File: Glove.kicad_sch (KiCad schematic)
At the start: 39 parts

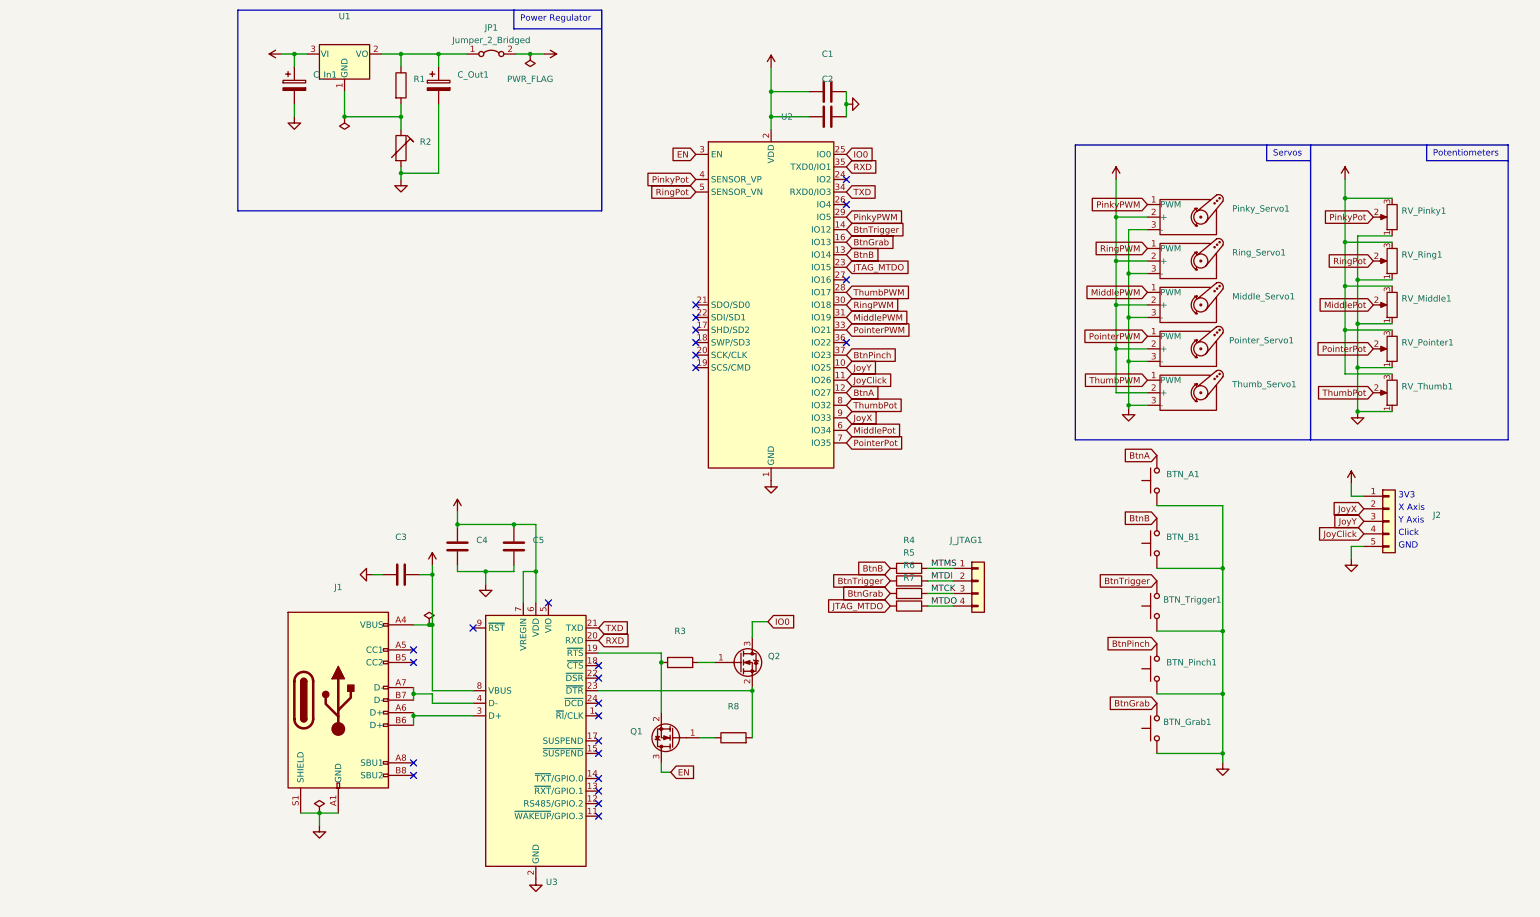
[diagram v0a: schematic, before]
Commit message: Remove Voltage Divider from Power Supply
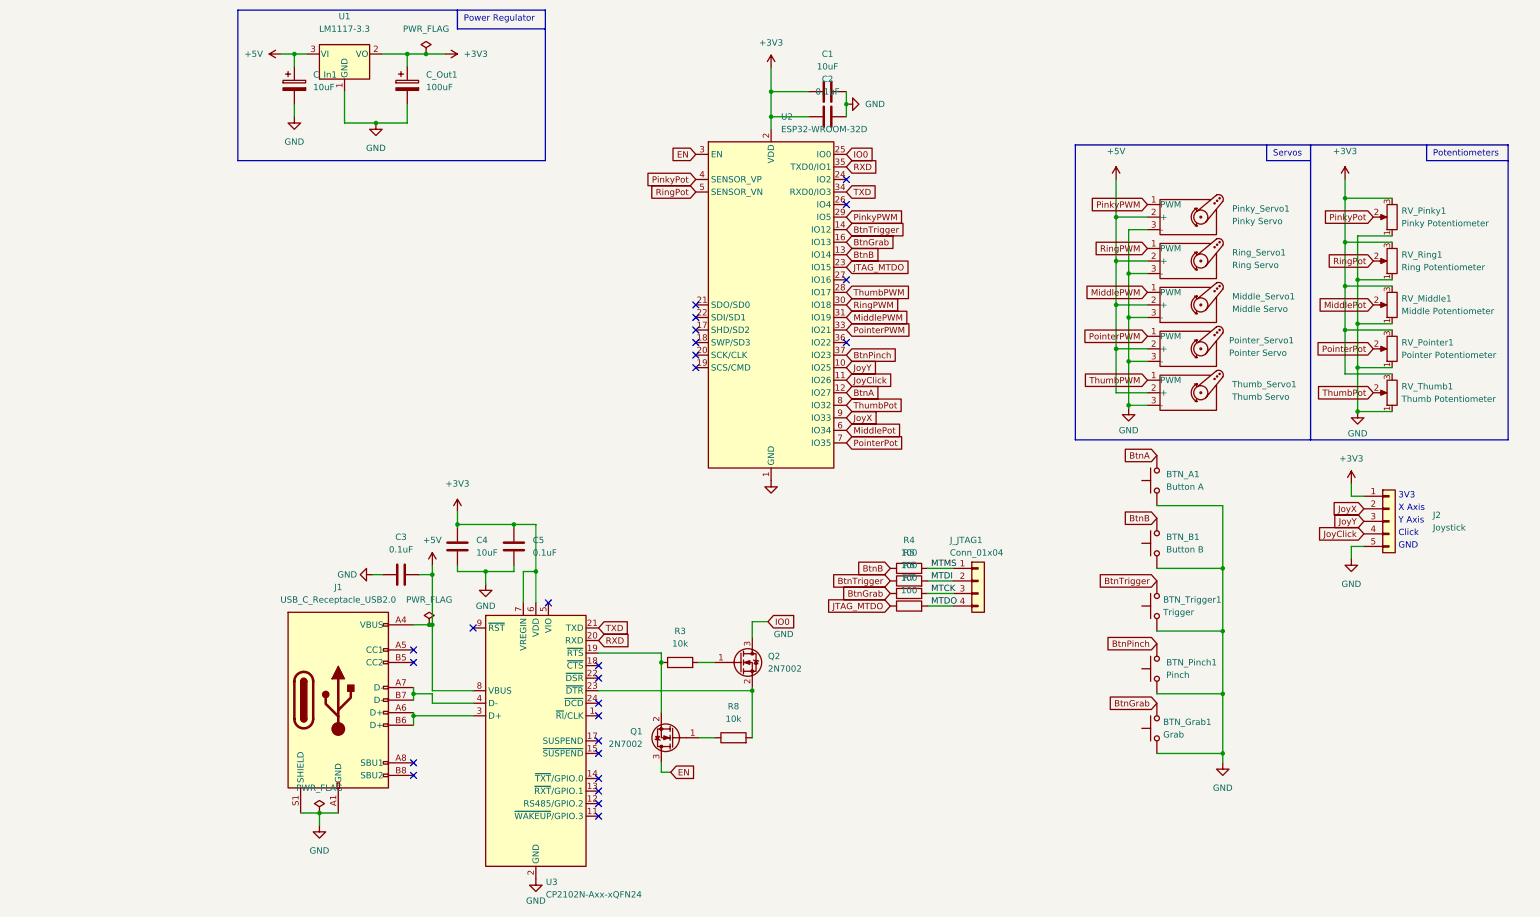
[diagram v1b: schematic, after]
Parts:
- removed JP1: Jumper_2_Bridged, Connector_PinHeader_2.54mm:PinHeader_1x02_P2.54mm_Vertical, symbol Jumper:Jumper_2_Bridged
- removed R1: (no value), symbol Device:R
- removed R2: (no value), symbol Device:R_Trim
- BTN_A1: value (none) -> Button A; footprint (none) -> Connector_JST:JST_XH_B2B-XH-A_1x02_P2.50mm_Vertical
- BTN_B1: value (none) -> Button B; footprint (none) -> Connector_JST:JST_XH_B2B-XH-A_1x02_P2.50mm_Vertical
- BTN_Grab1: value (none) -> Grab; footprint (none) -> Connector_JST:JST_XH_B2B-XH-A_1x02_P2.50mm_Vertical
- BTN_Pinch1: value (none) -> Pinch; footprint (none) -> Connector_JST:JST_XH_B2B-XH-A_1x02_P2.50mm_Vertical
- BTN_Trigger1: value (none) -> Trigger; footprint (none) -> Connector_JST:JST_XH_B2B-XH-A_1x02_P2.50mm_Vertical
- C1, C4, C_In1: value (none) -> 10uF; footprint (none) -> Capacitor_SMD:C_0805_2012Metric_Pad1.18x1.45mm_HandSolder
- C2, C3, C5: value (none) -> 0.1uF; footprint (none) -> Capacitor_SMD:C_0805_2012Metric_Pad1.18x1.45mm_HandSolder
- C_Out1: value (none) -> 100uF; footprint (none) -> Capacitor_SMD:C_0805_2012Metric_Pad1.18x1.45mm_HandSolder
- J1: value (none) -> USB_C_Receptacle_USB2.0; footprint (none) -> Connector_USB:USB_C_Receptacle_XKB_U262-16XN-4BVC11
- J2: value (none) -> Joystick; footprint (none) -> Connector_JST:JST_XH_B5B-XH-A_1x05_P2.50mm_Vertical
- J_JTAG1: value (none) -> Conn_01x04; footprint (none) -> Connector_PinHeader_2.54mm:PinHeader_1x04_P2.54mm_Vertical
- Middle_Servo1: value (none) -> Middle Servo; footprint (none) -> Connector_JST:JST_XH_B3B-XH-A_1x03_P2.50mm_Vertical
- Pinky_Servo1: value (none) -> Pinky Servo; footprint (none) -> Connector_JST:JST_XH_B3B-XH-A_1x03_P2.50mm_Vertical
- Pointer_Servo1: value (none) -> Pointer Servo; footprint (none) -> Connector_JST:JST_XH_B3B-XH-A_1x03_P2.50mm_Vertical
- Q1, Q2: value (none) -> 2N7002; footprint (none) -> Package_TO_SOT_SMD:SOT-23
- R3, R8: value (none) -> 10k; footprint (none) -> Resistor_SMD:R_0805_2012Metric_Pad1.20x1.40mm_HandSolder
- R4, R5, R6, R7: value (none) -> 100; footprint (none) -> Resistor_SMD:R_0805_2012Metric_Pad1.20x1.40mm_HandSolder
- RV_Middle1: value (none) -> Middle Potentiometer; footprint (none) -> Connector_JST:JST_XH_B3B-XH-A_1x03_P2.50mm_Vertical
- RV_Pinky1: value (none) -> Pinky Potentiometer; footprint (none) -> Connector_JST:JST_XH_B3B-XH-A_1x03_P2.50mm_Vertical
- RV_Pointer1: value (none) -> Pointer Potentiometer; footprint (none) -> Connector_JST:JST_XH_B3B-XH-A_1x03_P2.50mm_Vertical
- RV_Ring1: value (none) -> Ring Potentiometer; footprint (none) -> Connector_JST:JST_XH_B3B-XH-A_1x03_P2.50mm_Vertical
- RV_Thumb1: value (none) -> Thumb Potentiometer; footprint (none) -> Connector_JST:JST_XH_B3B-XH-A_1x03_P2.50mm_Vertical
- Ring_Servo1: value (none) -> Ring Servo; footprint (none) -> Connector_JST:JST_XH_B3B-XH-A_1x03_P2.50mm_Vertical
- Thumb_Servo1: value (none) -> Thumb Servo; footprint (none) -> Connector_JST:JST_XH_B3B-XH-A_1x03_P2.50mm_Vertical
- U1: value (none) -> LM1117-3.3; footprint (none) -> Package_TO_SOT_SMD:SOT-223
- U2: value (none) -> ESP32-WROOM-32D; footprint (none) -> RF_Module:ESP32-WROOM-32
- U3: value (none) -> CP2102N-Axx-xQFN24; footprint (none) -> Package_DFN_QFN:QFN-24-1EP_4x4mm_P0.5mm_EP2.6x2.6mm
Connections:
- net +3V3: now also C_Out1.1, U1.2 (VO)
- net GND: now also U1.1 (GND)
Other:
- moved on the sheet: C_Out1

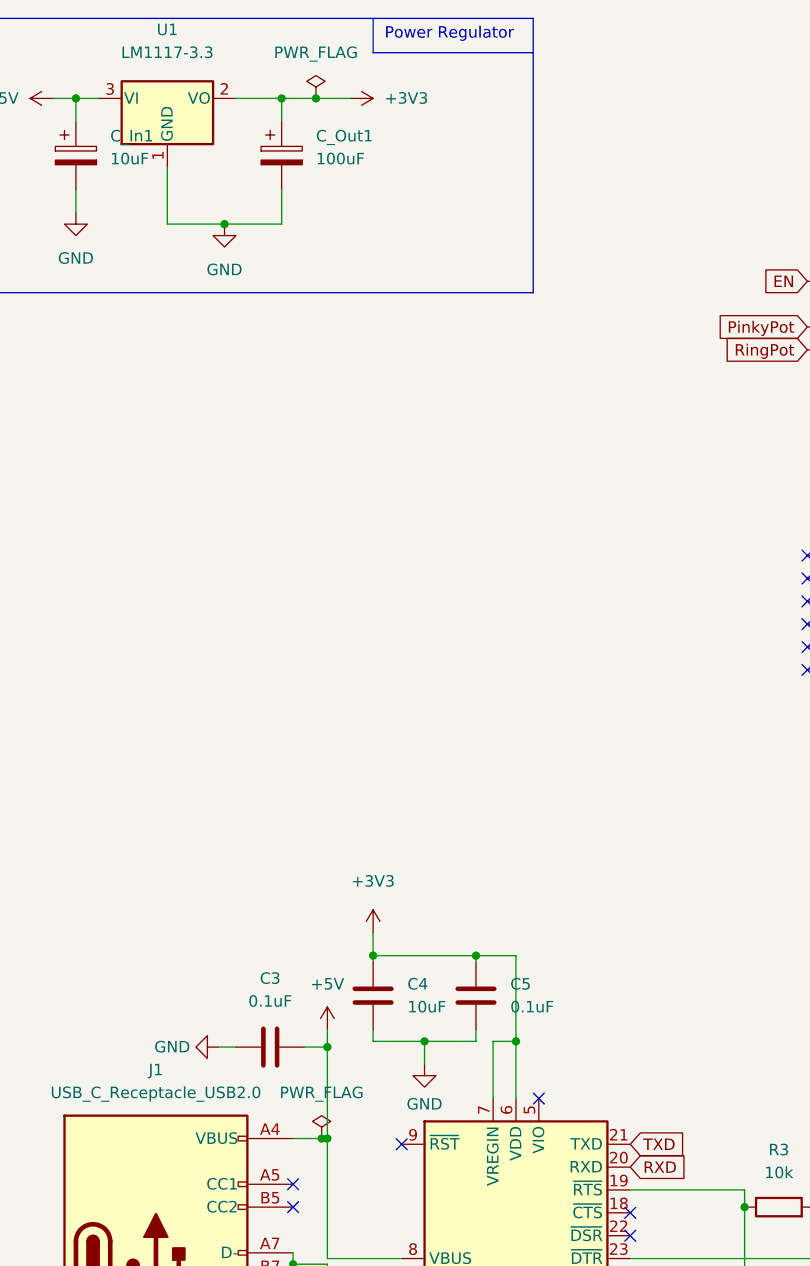
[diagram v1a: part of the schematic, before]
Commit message: Connect VIO to 3.3v for CP2102 chip
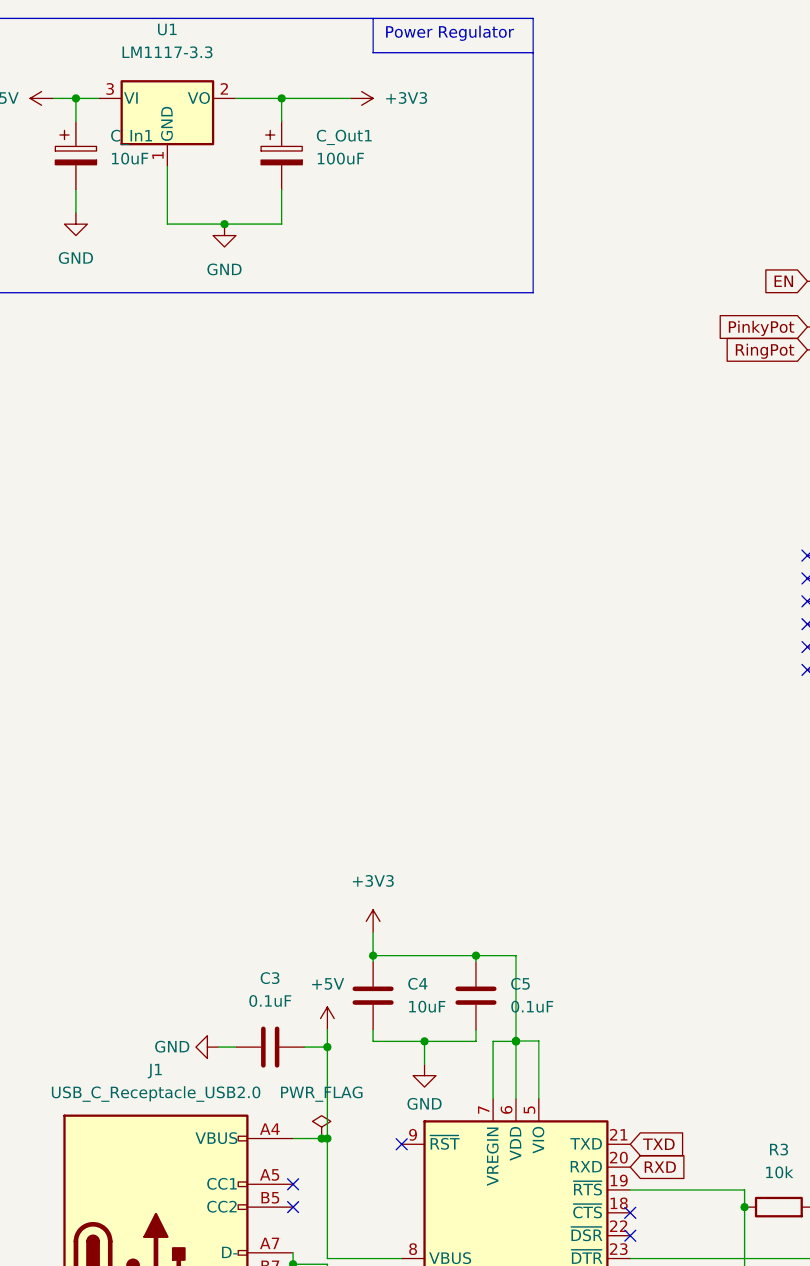
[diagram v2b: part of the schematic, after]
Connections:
- net +3V3: now also U3.5 (VIO)
- no-connect marks 26 -> 25
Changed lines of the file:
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@@
   (junction (at 234.315 50.8) (diameter 0) (color 0 0 0 0)
   )
-  (junction (at 48.26 21.59) (diameter 0) (color 0 0 0 0)
-  )
   (junction (at 26.67 175.26) (diameter 0) (color 0 0 0 0)
   )
   (junction (at 60.325 126.365) (diameter 0) (color 0 0 0 0)
+  )
+  (junction (at 70.485 126.3242) (diameter 0) (color 0 0 0 0)
   )
   (junction (at 236.855 85.09) (diameter 0) (color 0 0 0 0)
@@
   (no_connect (at 83.185 145.415))
   (no_connect (at 45.72 142.24))
-  (no_connect (at 73.025 132.715))
   (no_connect (at 83.185 153.035))
   (no_connect (at 83.185 170.815))
@@
     (stroke (width 0) (type default) (color 0 0 0 0))
   )
-  (wire (pts (xy 70.485 116.84) (xy 70.485 126.365))
+  (wire (pts (xy 70.485 116.84) (xy 70.485 126.3242))
     (stroke (width 0) (type default) (color 0 0 0 0))
   )
@@
     (stroke (width 0) (type default) (color 0 0 0 0))
   )
-  (wire (pts (xy 48.26 21.59) (xy 52.07 21.59))
-    (stroke (width 0) (type default) (color 0 0 0 0))
-  )
   (wire (pts (xy 19.05 21.59) (xy 21.59 21.59))
     (stroke (width 0) (type default) (color 0 0 0 0))
@@
     (stroke (width 0) (type default) (color 0 0 0 0))
   )
+  (wire (pts (xy 73.025 126.3242) (xy 73.025 132.715))
+    (stroke (width 0) (type default) (color 0 0 0 0))
+  )
   (wire (pts (xy 194.31 54.61) (xy 187.96 54.61))
     (stroke (width 0) (type default) (color 0 0 0 0))
@@
     (stroke (width 0) (type default) (color 0 0 0 0))
   )
+  (wire (pts (xy 70.485 126.3242) (xy 70.485 126.365))
+    (stroke (width 0) (type default) (color 0 0 0 0))
+  )
   (wire (pts (xy 46.99 127) (xy 49.53 127))
     (stroke (width 0) (type default) (color 0 0 0 0))
@@
     (stroke (width 0) (type default) (color 0 0 0 0))
   )
+  (wire (pts (xy 70.485 126.3242) (xy 73.025 126.3242))
+    (stroke (width 0) (type default) (color 0 0 0 0))
+  )
   (wire (pts (xy 26.67 175.26) (xy 26.67 177.8))
     (stroke (width 0) (type default) (color 0 0 0 0))
@@
     (stroke (width 0) (type default) (color 0 0 0 0))
   )
-  (wire (pts (xy 44.45 21.59) (xy 48.26 21.59))
+  (wire (pts (xy 44.45 21.59) (xy 52.07 21.59))
     (stroke (width 0) (type default) (color 0 0 0 0))
   )
@@
     (pin "1")
   )
-  (symbol (lib_id "power:PWR_FLAG") (at 48.26 21.59 0) (unit 1)
-    (in_bom yes) (on_board yes) (fields_autoplaced)
-    (property "Reference" "#FLG0102" (id 0) (at 48.26 19.685 0)
-      (effects (font (size 1.27 1.27)) hide)
-    )
-    (property "Value" "PWR_FLAG" (id 1) (at 48.26 16.51 0))
-    (property "Footprint" "" (id 2) (at 48.26 21.59 0)
-      (effects (font (size 1.27 1.27)) hide)
-    )
-    (property "Datasheet" "~" (id 3) (at 48.26 21.59 0)
-      (effects (font (size 1.27 1.27)) hide)
-    )
-    (pin "1")
-  )
   (symbol (lib_id "Device:R_Potentiometer") (at 243.84 90.17 180) (unit 1)
     (in_bom yes) (on_board yes) (fields_autoplaced)
@@
       (reference "#FLG02") (unit 1) (value "PWR_FLAG") (footprint "")
     )
-    (path "/609d9915-16aa-47b0-bfbf-4aec5d0417ef"
-      (reference "#FLG0102") (unit 1) (value "PWR_FLAG") (footprint "")
-    )
     (path "/68620e30-8afe-4ab3-b736-a9681346ab55"
